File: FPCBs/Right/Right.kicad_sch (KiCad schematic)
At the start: 20 parts, among them J1 PCB, J4 shutter+1st_dial, SW1 Mode Dial, SW2 ON/OFF, SW3 Focus+Shutter, U1 SG-105, U2 SG-105

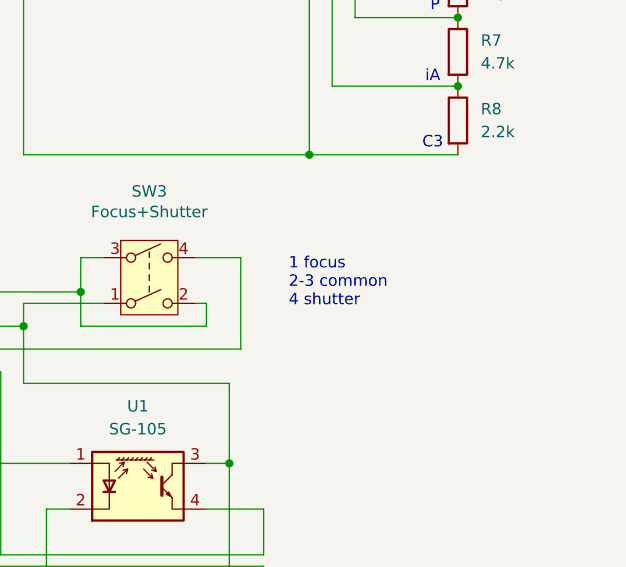
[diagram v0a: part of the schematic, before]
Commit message: Add second shutter
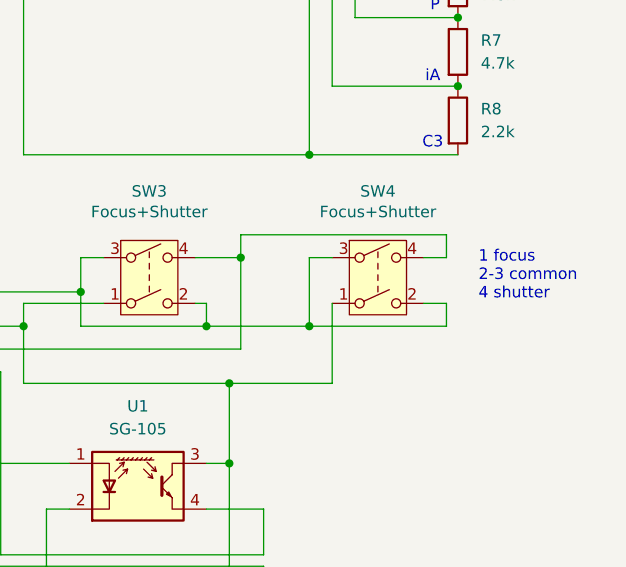
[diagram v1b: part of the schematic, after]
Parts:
- added SW4: Focus+Shutter, Leica-G9ii:Shutter_Olympus, symbol Switch:SW_DPST
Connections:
- net at J1.23 (Pin_23), J1.24 (Pin_24), J4.2 (Pin_2)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: now also SW4.1
- net at J1.25 (Pin_25), J4.3 (Pin_3), SW3.4: now also SW4.4
- net at J1.26 (Pin_26), J4.1 (Pin_1), SW3.2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: now also SW4.2, SW4.3
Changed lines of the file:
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@@
 	(text "1 focus\n2-3 common\n4 shutter"
 		(exclude_from_sim no)
-		(at 178.054 106.934 0)
+		(at 199.136 106.172 0)
 		(effects
 			(font
@@
 	)
 	(junction
+		(at 171.45 118.11)
+		(diameter 0)
+		(color 0 0 0 0)
+	)
+	(junction
 		(at 78.74 62.23)
 		(diameter 0)
@@
 	)
 	(junction
+		(at 180.34 111.76)
+		(diameter 0)
+		(color 0 0 0 0)
+	)
+	(junction
+		(at 168.91 111.76)
+		(diameter 0)
+		(color 0 0 0 0)
+	)
+	(junction
 		(at 132.08 111.76)
 		(diameter 0)
@@
 		(color 0 0 0 0)
 	)
+	(junction
+		(at 172.72 104.14)
+		(diameter 0)
+		(color 0 0 0 0)
+	)
 	(wire
 		(pts
@@
 	(wire
 		(pts
+			(xy 195.58 104.14) (xy 195.58 101.6)
+		)
+		(stroke
+			(width 0)
+			(type default)
+		)
+	)
+	(wire
+		(pts
 			(xy 93.98 78.74) (xy 76.2 78.74)
 		)
@@
 	(wire
 		(pts
+			(xy 182.88 109.22) (xy 182.88 118.11)
+		)
+		(stroke
+			(width 0)
+			(type default)
+		)
+	)
+	(wire
+		(pts
 			(xy 93.98 76.2) (xy 93.98 74.93)
 		)
@@
 	(wire
 		(pts
+			(xy 180.34 104.14) (xy 180.34 111.76)
+		)
+		(stroke
+			(width 0)
+			(type default)
+		)
+	)
+	(wire
+		(pts
 			(xy 73.66 76.2) (xy 93.98 76.2)
 		)
@@
 	(wire
 		(pts
+			(xy 182.88 104.14) (xy 180.34 104.14)
+		)
+		(stroke
+			(width 0)
+			(type default)
+		)
+	)
+	(wire
+		(pts
 			(xy 78.74 109.22) (xy 93.98 109.22)
 		)
@@
 	(wire
 		(pts
+			(xy 195.58 101.6) (xy 172.72 101.6)
+		)
+		(stroke
+			(width 0)
+			(type default)
+		)
+	)
+	(wire
+		(pts
 			(xy 151.13 132.08) (xy 151.13 148.59)
 		)
@@
 	(wire
 		(pts
+			(xy 180.34 111.76) (xy 195.58 111.76)
+		)
+		(stroke
+			(width 0)
+			(type default)
+		)
+	)
+	(wire
+		(pts
 			(xy 148.59 92.71) (xy 148.59 59.69)
 		)
@@
 	(wire
 		(pts
+			(xy 168.91 111.76) (xy 180.34 111.76)
+		)
+		(stroke
+			(width 0)
+			(type default)
+		)
+	)
+	(wire
+		(pts
 			(xy 185.42 77.47) (xy 185.42 62.23)
 		)
@@
 	(wire
 		(pts
+			(xy 172.72 101.6) (xy 172.72 104.14)
+		)
+		(stroke
+			(width 0)
+			(type default)
+		)
+	)
+	(wire
+		(pts
+			(xy 195.58 111.76) (xy 195.58 109.22)
+		)
+		(stroke
+			(width 0)
+			(type default)
+		)
+	)
+	(wire
+		(pts
 			(xy 96.52 118.11) (xy 52.07 118.11)
 		)
@@
 	(wire
 		(pts
+			(xy 182.88 118.11) (xy 171.45 118.11)
+		)
+		(stroke
+			(width 0)
+			(type default)
+		)
+	)
+	(wire
+		(pts
 			(xy 175.26 138.43) (xy 175.26 153.67)
 		)
@@
 	(wire
 		(pts
+			(xy 195.58 109.22) (xy 193.04 109.22)
+		)
+		(stroke
+			(width 0)
+			(type default)
+		)
+	)
+	(wire
+		(pts
 			(xy 175.26 137.16) (xy 146.05 137.16)
 		)
@@
 	(wire
 		(pts
+			(xy 193.04 104.14) (xy 195.58 104.14)
+		)
+		(stroke
+			(width 0)
+			(type default)
+		)
+	)
+	(wire
+		(pts
 			(xy 78.74 59.69) (xy 78.74 58.42)
 		)
@@
 		)
 	)
+	(symbol
+		(lib_id "Switch:SW_DPST")
+		(at 187.96 106.68 0)
+		(unit 1)
+		(exclude_from_sim no)
+		(in_bom yes)
+		(on_board yes)
+		(dnp no)
+		(property "Reference" "SW4"
+			(at 187.96 96.774 0)
+			(effects
+				(font
+					(size 1.27 1.27)
+				)
+			)
+		)
+		(property "Value" "Focus+Shutter"
+			(at 187.96 99.06 0)
+			(effects
+				(font
+					(size 1.27 1.27)
+				)
+			)
+		)
+		(property "Footprint" "Leica-G9ii:Shutter_Olympus"
+			(at 187.96 106.68 0)
+			(effects
+				(font
+					(size 1.27 1.27)
+				)
+				(hide yes)
+			)
+		)
+		(property "Datasheet" "~"
+			(at 187.96 106.68 0)
+			(effects
+				(font
+					(size 1.27 1.27)
+				)
+				(hide yes)
+			)
+		)
+		(property "Description" "Double Pole Single Throw (DPST) Switch"
+			(at 187.96 106.68 0)
+			(effects
+				(font
+					(size 1.27 1.27)
+				)
+				(hide yes)
+			)
+		)
+		(pin "3"
+		)
+		(pin "2"
+		)
+		(pin "4"
+		)
+		(pin "1"
+		)
+		(instances
+			(project "Right"
+				(path "/4f08b7d7-0978-402f-8bca-f87716f6be32"
+					(reference "SW4")
+					(unit 1)
+				)
+			)
+		)
+	)

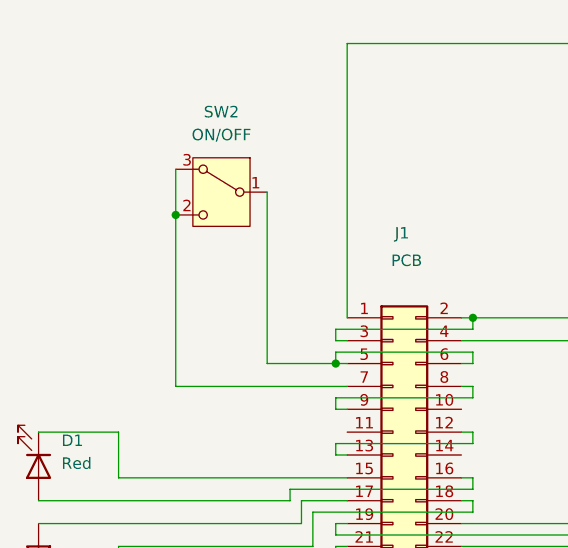
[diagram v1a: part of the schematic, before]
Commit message: Add second power button
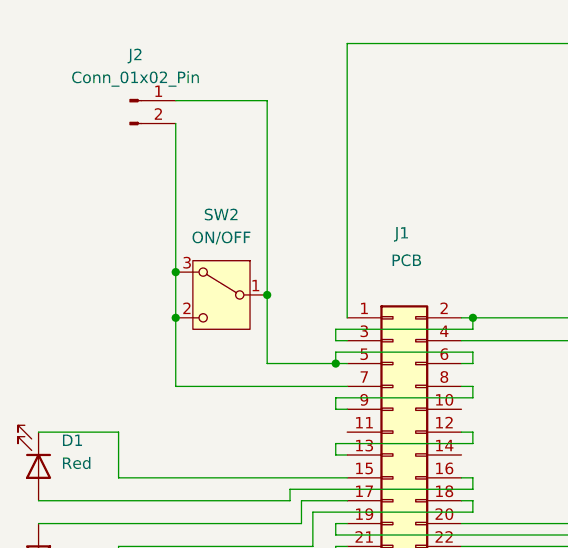
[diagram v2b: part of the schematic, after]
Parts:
- added J2: Conn_01x02_Pin, Leica-G9ii:Connector-Screw-2Pins, symbol Connector:Conn_01x02_Pin
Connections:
- net at J1.5 (Pin_5), J1.6 (Pin_6), SW2.1 (B): now also J2.1 (Pin_1)
- net at J1.7 (Pin_7), SW2.2 (C), SW2.3 (A): now also J2.2 (Pin_2)
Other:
- moved on the sheet: SW2
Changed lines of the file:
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@@
 	)
 	(junction
-		(at 60.96 45.72)
+		(at 60.96 57.15)
 		(diameter 0)
 		(color 0 0 0 0)
@@
 	)
 	(junction
+		(at 71.12 54.61)
+		(diameter 0)
+		(color 0 0 0 0)
+	)
+	(junction
 		(at 180.34 92.71)
 		(diameter 0)
@@
 	)
 	(junction
+		(at 60.96 52.07)
+		(diameter 0)
+		(color 0 0 0 0)
+	)
+	(junction
 		(at 172.72 104.14)
 		(diameter 0)
@@
 	(wire
 		(pts
+			(xy 71.12 33.02) (xy 71.12 54.61)
+		)
+		(stroke
+			(width 0)
+			(type default)
+		)
+	)
+	(wire
+		(pts
 			(xy 93.98 86.36) (xy 93.98 85.09)
 		)
@@
 	(wire
 		(pts
+			(xy 60.96 57.15) (xy 60.96 52.07)
+		)
+		(stroke
+			(width 0)
+			(type default)
+		)
+	)
+	(wire
+		(pts
 			(xy 101.6 114.3) (xy 132.08 114.3)
 		)
@@
 	(wire
 		(pts
-			(xy 121.92 87.63) (xy 121.92 109.22)
+			(xy 60.96 35.56) (xy 60.96 52.07)
 		)
 		(stroke
@@
 	(wire
 		(pts
-			(xy 182.88 104.14) (xy 180.34 104.14)
+			(xy 121.92 87.63) (xy 121.92 109.22)
 		)
 		(stroke
@@
 	(wire
 		(pts
-			(xy 78.74 109.22) (xy 93.98 109.22)
+			(xy 182.88 104.14) (xy 180.34 104.14)
 		)
 		(stroke
@@
 	(wire
 		(pts
-			(xy 135.89 124.46) (xy 132.08 124.46)
+			(xy 78.74 109.22) (xy 93.98 109.22)
 		)
 		(stroke
@@
 	(wire
 		(pts
-			(xy 104.14 111.76) (xy 132.08 111.76)
+			(xy 135.89 124.46) (xy 132.08 124.46)
 		)
 		(stroke
@@
 	(wire
 		(pts
-			(xy 60.96 45.72) (xy 60.96 64.77)
+			(xy 104.14 111.76) (xy 132.08 111.76)
 		)
 		(stroke
@@
 	(wire
 		(pts
-			(xy 71.12 43.18) (xy 71.12 62.23)
+			(xy 71.12 54.61) (xy 71.12 62.23)
 		)
 		(stroke
@@
 	(wire
 		(pts
-			(xy 60.96 40.64) (xy 60.96 45.72)
-		)
-		(stroke
-			(width 0)
-			(type default)
-		)
-	)
-	(wire
-		(pts
 			(xy 78.74 86.36) (xy 78.74 85.09)
 		)
@@
 	(wire
 		(pts
+			(xy 60.96 57.15) (xy 60.96 64.77)
+		)
+		(stroke
+			(width 0)
+			(type default)
+		)
+	)
+	(wire
+		(pts
 			(xy 93.98 62.23) (xy 93.98 60.96)
 		)
@@
 	(wire
 		(pts
+			(xy 60.96 33.02) (xy 71.12 33.02)
+		)
+		(stroke
+			(width 0)
+			(type default)
+		)
+	)
+	(wire
+		(pts
 			(xy 171.45 127) (xy 168.91 127)
 		)
@@
 	)
 	(symbol
+		(lib_id "Connector:Conn_01x02_Pin")
+		(at 55.88 33.02 0)
+		(unit 1)
+		(exclude_from_sim no)
+		(in_bom yes)
+		(on_board yes)
+		(dnp no)
+		(fields_autoplaced yes)
+		(property "Reference" "J2"
+			(at 56.515 27.94 0)
+			(effects
+				(font
+					(size 1.27 1.27)
+				)
+			)
+		)
+		(property "Value" "Conn_01x02_Pin"
+			(at 56.515 30.48 0)
+			(effects
+				(font
+					(size 1.27 1.27)
+				)
+			)
+		)
+		(property "Footprint" "Leica-G9ii:Connector-Screw-2Pins"
+			(at 55.88 33.02 0)
+			(effects
+				(font
+					(size 1.27 1.27)
+				)
+				(hide yes)
+			)
+		)
+		(property "Datasheet" "~"
+			(at 55.88 33.02 0)
+			(effects
+				(font
+					(size 1.27 1.27)
+				)
+				(hide yes)
+			)
+		)
+		(property "Description" "Generic connector, single row, 01x02, script generated"
+			(at 55.88 33.02 0)
+			(effects
+				(font
+					(size 1.27 1.27)
+				)
+				(hide yes)
+			)
+		)
+		(pin "1"
+		)
+		(pin "2"
+		)
+		(instances
+			(project ""
+				(path "/4f08b7d7-0978-402f-8bca-f87716f6be32"
+					(reference "J2")
+					(unit 1)
+				)
+			)
+		)
+	)
+	(symbol
 		(lib_id "Device:R_Potentiometer")
 		(at 74.93 109.22 0)
@@
 	(symbol
 		(lib_id "Switch:SW_SPDT_312")
-		(at 66.04 43.18 0)
+		(at 66.04 54.61 0)
 		(mirror y)
 		(unit 1)
@@
 		(fields_autoplaced yes)
 		(property "Reference" "SW2"
-			(at 66.04 34.29 0)
+			(at 66.04 45.72 0)
 			(effects
 				(font
@@
 		)
 		(property "Value" "ON/OFF"
-			(at 66.04 36.83 0)
+			(at 66.04 48.26 0)
 			(effects
 				(font
@@
 		)
 		(property "Footprint" "Leica-G9ii:Switch_ON_OFF"
-			(at 66.04 53.34 0)
+			(at 66.04 64.77 0)
 			(effects
 				(font
@@
 		)
 		(property "Datasheet" "~"
-			(at 66.04 50.8 0)
+			(at 66.04 62.23 0)
 			(effects
 				(font
@@
 		)
 		(property "Description" "Switch, single pole double throw"
-			(at 66.04 43.18 0)
+			(at 66.04 54.61 0)
 			(effects
 				(font

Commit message: Adjustments for evf and right fpcb
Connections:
- net at J1.32 (Pin_32): now also BT1.1 (+); no longer BT1.2 (-)
- net at R9.2: now also BT1.2 (-); no longer BT1.1 (+)
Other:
- moved on the sheet: BT1
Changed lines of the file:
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@@
 	(symbol
 		(lib_id "Device:Battery_Cell")
-		(at 52.07 111.76 0)
+		(at 52.07 109.22 180)
 		(unit 1)
 		(exclude_from_sim no)
@@
 		(dnp no)
 		(property "Reference" "BT1"
-			(at 44.704 110.744 0)
+			(at 59.436 110.236 0)
 			(effects
 				(font
@@
 		)
 		(property "Value" "2.6V"
-			(at 43.688 113.03 0)
+			(at 60.452 107.95 0)
 			(effects
 				(font
@@
 		)
 		(property "Footprint" "Leica-G9ii:Battery_Cell"
-			(at 52.07 110.236 90)
+			(at 52.07 110.744 90)
 			(effects
 				(font
@@
 		)
 		(property "Datasheet" "~"
-			(at 52.07 110.236 90)
+			(at 52.07 110.744 90)
 			(effects
 				(font
@@
 		)
 		(property "Description" "Single-cell battery"
-			(at 52.07 111.76 0)
+			(at 52.07 109.22 0)
 			(effects
 				(font
